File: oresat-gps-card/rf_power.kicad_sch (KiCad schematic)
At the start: 26 parts, among them U15 SKY65723-81, U16 BP2G+, U17 MAX8510EXK29+T, U18 MAX8510EXK29+T, U19 MAX8510EXK33+T

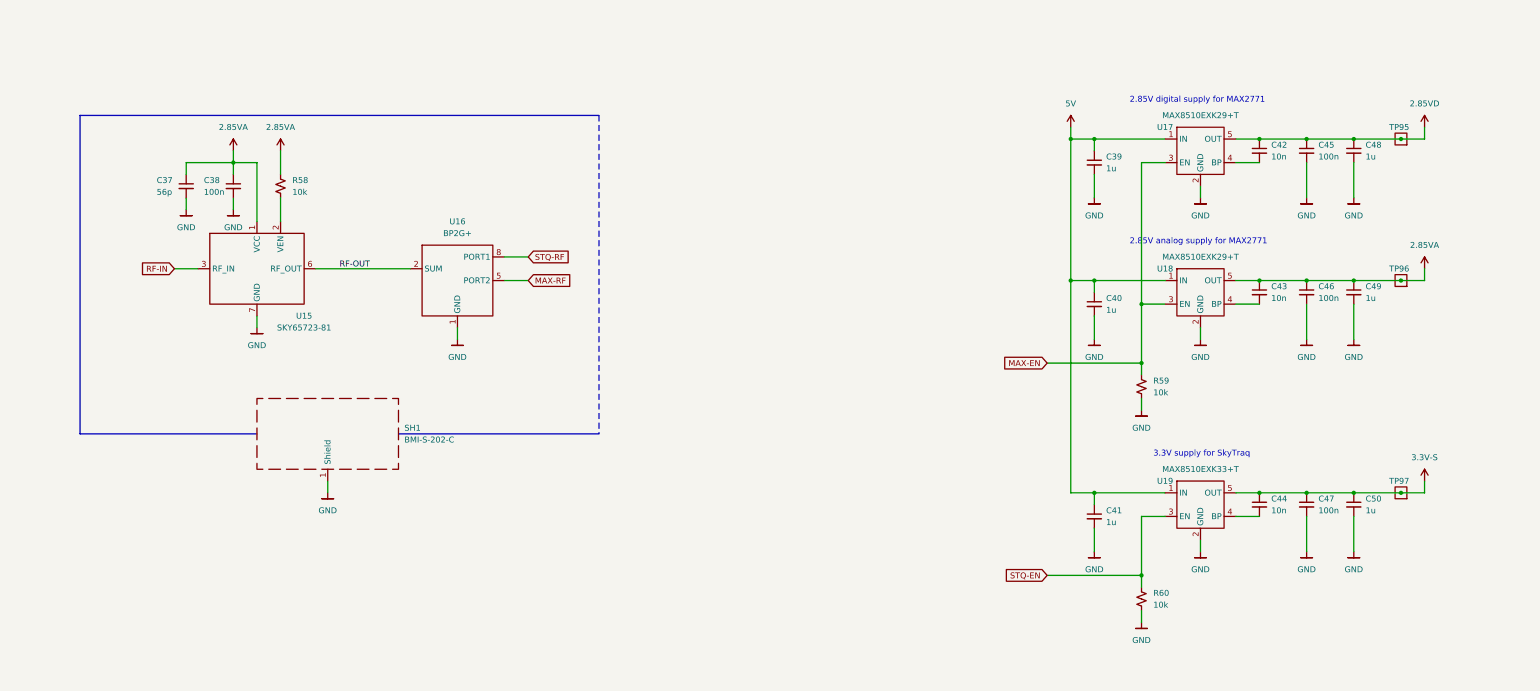
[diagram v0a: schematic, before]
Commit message: GPS card design review changes and issue fixes
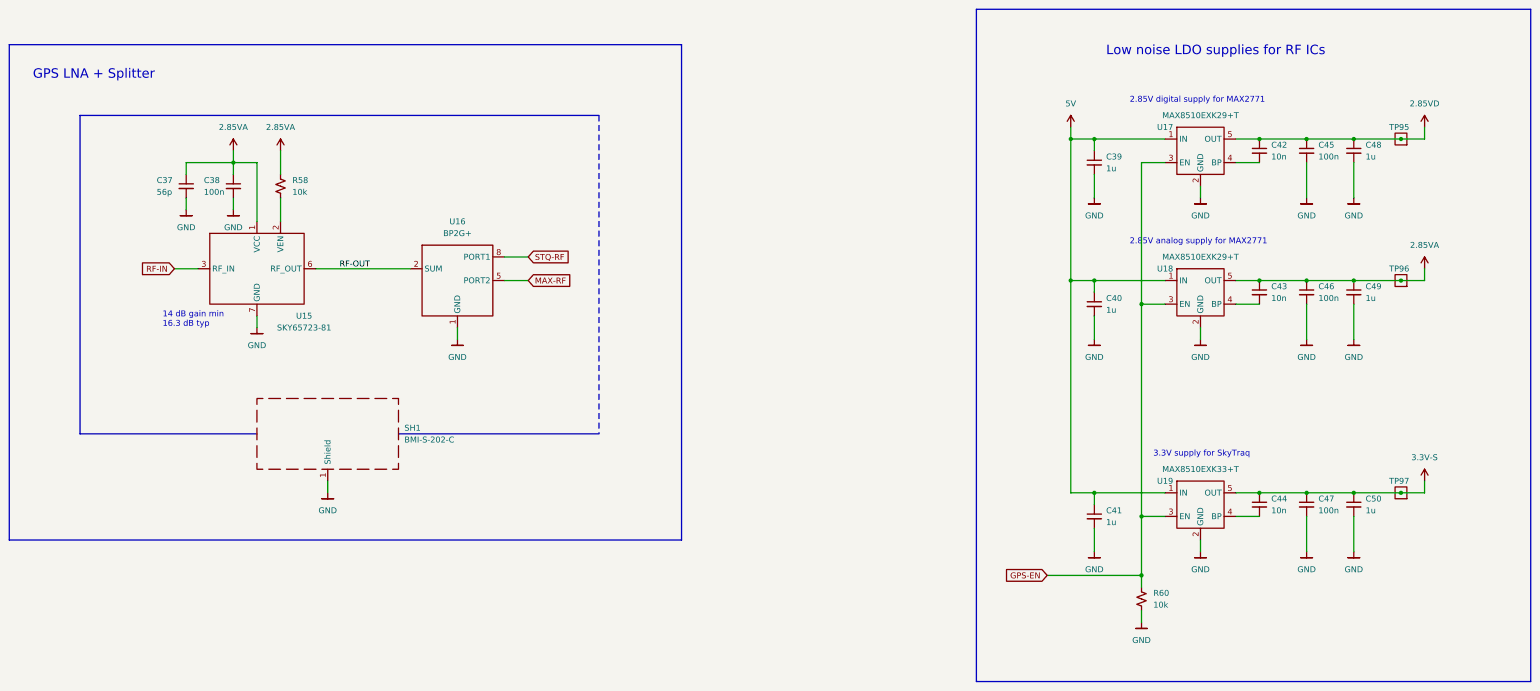
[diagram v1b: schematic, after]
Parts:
- removed R59: 10k, Resistor_SMD:R_0603_1608Metric, symbol Device:R_Small_US
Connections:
- net STQ-EN is gone; now on net GPS-EN: R60.1, U19.3 (EN)
- net MAX-EN renamed GPS-EN
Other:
- note added: "14 dB gain min 16.3 dB typ"
- note added: "GPS LNA + Splitter"
- note added: "Low noise LDO supplies for RF ICs"
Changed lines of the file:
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@@
   (junction (at 325.12 73.66) (diameter 0) (color 0 0 0 0)
   )
-  (junction (at 289.56 121.92) (diameter 0) (color 0 0 0 0)
+  (junction (at 289.56 154.94) (diameter 0) (color 0 0 0 0)
   )
   (junction (at 345.44 149.86) (diameter 0) (color 0 0 0 0)
@@
     (stroke (width 0) (type default) (color 0 0 0 0))
   )
-  (wire (pts (xy 269.24 121.92) (xy 289.56 121.92))
-    (stroke (width 0) (type default) (color 0 0 0 0))
-  )
   (wire (pts (xy 274.32 73.66) (xy 274.32 71.12))
     (stroke (width 0) (type default) (color 0 0 0 0))
@@
     (stroke (width 0) (type default) (color 0 0 0 0))
   )
+  (polyline (pts (xy 45.72 160.02) (xy 45.72 53.34))
+    (stroke (width 0) (type default) (color 0 0 0 0))
+  )
   (wire (pts (xy 93.98 78.74) (xy 99.06 78.74))
     (stroke (width 0) (type default) (color 0 0 0 0))
@@
     (stroke (width 0) (type default) (color 0 0 0 0))
   )
+  (polyline (pts (xy 373.38 190.5) (xy 373.38 45.72))
+    (stroke (width 0) (type default) (color 0 0 0 0))
+  )
   (wire (pts (xy 279.4 149.86) (xy 274.32 149.86))
     (stroke (width 0) (type default) (color 0 0 0 0))
@@
     (stroke (width 0) (type default) (color 0 0 0 0))
   )
+  (polyline (pts (xy 254 190.5) (xy 373.38 190.5))
+    (stroke (width 0) (type default) (color 0 0 0 0))
+  )
   (wire (pts (xy 335.28 109.22) (xy 335.28 116.84))
     (stroke (width 0) (type default) (color 0 0 0 0))
@@
     (stroke (width 0) (type default) (color 0 0 0 0))
   )
-  (wire (pts (xy 289.56 121.92) (xy 289.56 124.46))
+  (polyline (pts (xy 373.38 45.72) (xy 254 45.72))
     (stroke (width 0) (type default) (color 0 0 0 0))
   )
@@
     (stroke (width 0) (type default) (color 0 0 0 0))
   )
+  (polyline (pts (xy 190.5 53.34) (xy 190.5 160.02))
+    (stroke (width 0) (type default) (color 0 0 0 0))
+  )
   (wire (pts (xy 335.28 154.94) (xy 335.28 162.56))
     (stroke (width 0) (type default) (color 0 0 0 0))
@@
     (stroke (width 0) (type default) (color 0 0 0 0))
   )
-  (wire (pts (xy 289.56 109.22) (xy 289.56 121.92))
+  (wire (pts (xy 289.56 109.22) (xy 289.56 154.94))
     (stroke (width 0) (type default) (color 0 0 0 0))
   )
@@
   )
   (wire (pts (xy 279.4 76.2) (xy 279.4 73.66))
+    (stroke (width 0) (type default) (color 0 0 0 0))
+  )
+  (polyline (pts (xy 254 45.72) (xy 254 190.5))
     (stroke (width 0) (type default) (color 0 0 0 0))
   )
@@
     (stroke (width 0) (type default) (color 0 0 0 0))
   )
+  (polyline (pts (xy 45.72 160.02) (xy 190.5 160.02))
+    (stroke (width 0) (type default) (color 0 0 0 0))
+  )
   (wire (pts (xy 309.88 78.74) (xy 314.96 78.74))
     (stroke (width 0) (type default) (color 0 0 0 0))
@@
     (stroke (width 0) (type default) (color 0 0 0 0))
   )
+  (polyline (pts (xy 45.72 53.34) (xy 190.5 53.34))
+    (stroke (width 0) (type default) (color 0 0 0 0))
+  )
   (wire (pts (xy 99.06 78.74) (xy 99.06 91.44))
     (stroke (width 0) (type default) (color 0 0 0 0))
@@
   )
   (wire (pts (xy 152.4 104.14) (xy 157.48 104.14))
-    (stroke (width 0) (type default) (color 0 0 0 0))
-  )
-  (wire (pts (xy 289.56 129.54) (xy 289.56 132.08))
     (stroke (width 0) (type default) (color 0 0 0 0))
   )
@@
     (effects (font (size 1.27 1.27)) (justify left bottom))
   )
+  (text "Low noise LDO supplies for RF ICs" (at 281.94 55.88 0)
+    (effects (font (size 2.032 2.032)) (justify left bottom))
+  )
   (text "2.85V analog supply for MAX2771" (at 287.02 96.52 0)
     (effects (font (size 1.27 1.27)) (justify left bottom))
+  )
+  (text "14 dB gain min\n16.3 dB typ" (at 78.74 114.3 0)
+    (effects (font (size 1.27 1.27)) (justify left bottom))
+  )
+  (text "GPS LNA + Splitter" (at 50.8 60.96 0)
+    (effects (font (size 2.032 2.032)) (justify left bottom))
   )
   (label "RF-OUT" (at 116.84 101.6 0)
@@
     )
   )
-  (global_label "STQ-EN" (shape input) (at 269.24 167.64 180) (fields_autoplaced)
+  (global_label "GPS-EN" (shape input) (at 269.24 167.64 180) (fields_autoplaced)
     (effects (font (size 1.27 1.27)) (justify right))
-    (property "Intersheet References" "${INTERSHEET_REFS}" (id 0) (at 259.2674 167.5606 0)
-      (effects (font (size 1.27 1.27)) (justify right) hide)
-    )
-  )
-  (global_label "MAX-EN" (shape input) (at 269.24 121.92 180) (fields_autoplaced)
-    (effects (font (size 1.27 1.27)) (justify right))
-    (property "Intersheet References" "${INTERSHEET_REFS}" (id 0) (at 259.0255 121.8406 0)
+    (property "Intersheet References" "${INTERSHEET_REFS}" (id 0) (at 259.0255 167.5606 0)
       (effects (font (size 1.27 1.27)) (justify right) hide)
     )
@@
     (pin "5")
   )
-  (symbol (lib_id "OreSat-Power:GND") (at 289.56 132.08 0) (unit 1)
-    (in_bom yes) (on_board yes) (fields_autoplaced)
-    (property "Reference" "#GND0183" (id 0) (at 289.56 138.43 0)
-      (effects (font (size 1.27 1.27)) hide)
-    )
-    (property "Value" "GND" (id 1) (at 289.56 135.89 0))
-    (property "Footprint" "" (id 2) (at 289.56 132.08 0)
-      (effects (font (size 1.27 1.27)) hide)
-    )
-    (property "Datasheet" "" (id 3) (at 289.56 132.08 0)
-      (effects (font (size 1.27 1.27)) hide)
-    )
-    (pin "1")
-  )
   (symbol (lib_id "Device:C_Small") (at 325.12 152.4 0) (unit 1)
     (in_bom yes) (on_board yes) (fields_autoplaced)
@@
       (effects (font (size 1.27 1.27)) hide)
     )
-    (pin "1")
-    (pin "2")
-  )
-  (symbol (lib_id "Device:R_Small_US") (at 289.56 127 0) (unit 1)
-    (in_bom yes) (on_board yes) (fields_autoplaced)
-    (property "Reference" "R59" (id 0) (at 292.1 125.7299 0)
-      (effects (font (size 1.27 1.27)) (justify left))
-    )
-    (property "Value" "10k" (id 1) (at 292.1 128.2699 0)
-      (effects (font (size 1.27 1.27)) (justify left))
-    )
-    (property "Footprint" "Resistor_SMD:R_0603_1608Metric" (id 2) (at 289.56 127 0)
-      (effects (font (size 1.27 1.27)) hide)
-    )
-    (property "Datasheet" "~" (id 3) (at 289.56 127 0)
-      (effects (font (size 1.27 1.27)) hide)
-    )
